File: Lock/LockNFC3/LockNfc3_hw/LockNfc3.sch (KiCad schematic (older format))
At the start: 118 parts, among them Q1 IRLML9303, Q2 BC817, Q3 IRLML6302, Q4 IRLML6302, Q5 IRLML6302, Q6 LED_RGB, Q7 LED_RGB, Q8 LED_RGB, SW1 SS9, SW2 BUTTON, SW3 BUTTON, SW4 BUTTON

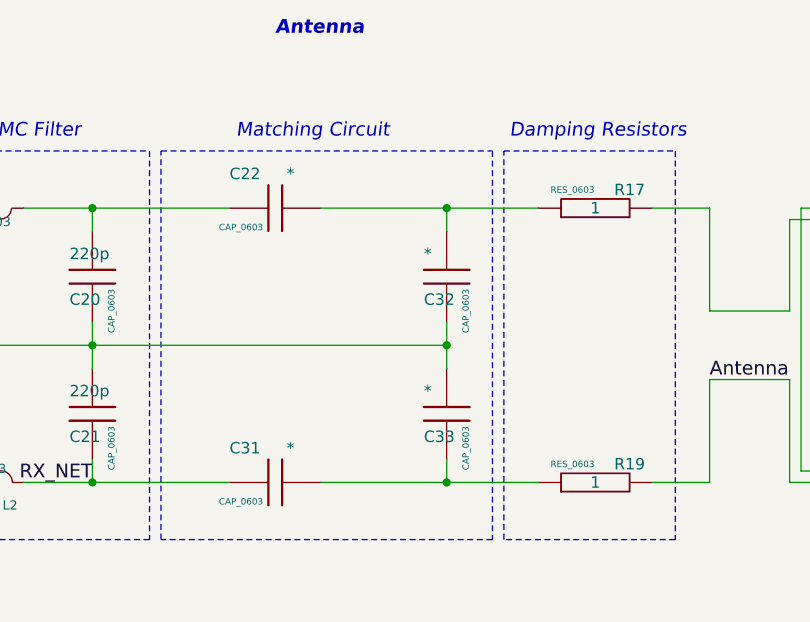
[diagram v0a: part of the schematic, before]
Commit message: * Capacitors values added
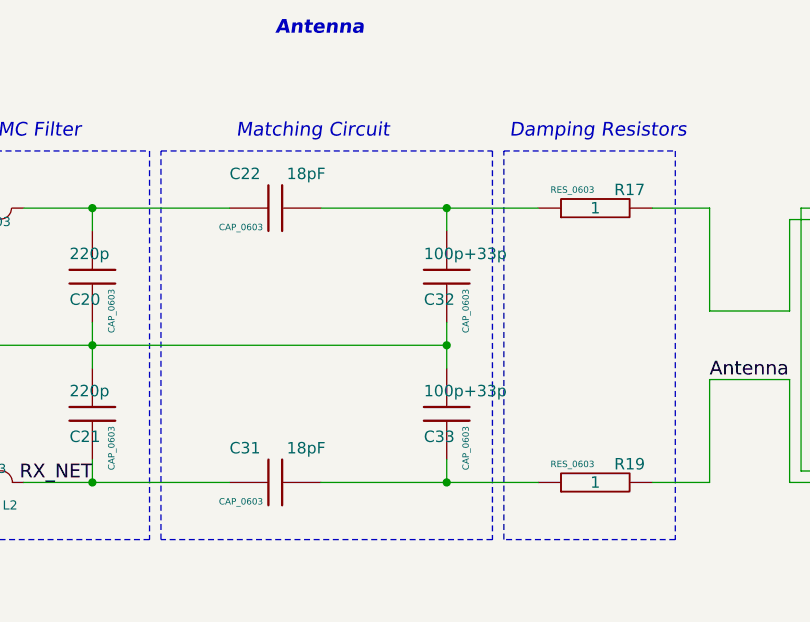
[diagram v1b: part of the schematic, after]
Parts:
- C22, C31: value * -> 18pF
- C32, C33: value * -> 100p+33p
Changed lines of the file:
@@
 Sheet 1 1
 Title ""
-Date "3 dec 2014"
+Date "24 feb 2015"
 Rev ""
 Comp ""
@@
 P 14150 3200
 F 0 "C33" H 14050 3100 50  0000 L CNN
-F 1 "*" H 14050 3300 50  0000 L CNN
+F 1 "100p+33p" H 14050 3300 50  0000 L CNN
 F 2 "CAP_0603" V 14250 3050 28  0000 C BNN
 F 3 "" H 14150 3200 60  0001 C CNN
@@
 P 14150 2600
 F 0 "C32" H 14050 2500 50  0000 L CNN
-F 1 "*" H 14050 2700 50  0000 L CNN
+F 1 "100p+33p" H 14050 2700 50  0000 L CNN
 F 2 "CAP_0603" V 14250 2450 28  0000 C BNN
 F 3 "" H 14150 2600 60  0001 C CNN
@@
 P 13400 3500
 F 0 "C31" V 13250 3300 50  0000 L CNN
-F 1 "*" V 13250 3550 50  0000 L CNN
+F 1 "18pF" V 13250 3550 50  0000 L CNN
 F 2 "CAP_0603" V 13500 3350 28  0000 C BNN
 F 3 "" H 13400 3500 60  0001 C CNN
@@
 P 13400 2300
 F 0 "C22" V 13250 2100 50  0000 L CNN
-F 1 "*" V 13250 2350 50  0000 L CNN
+F 1 "18pF" V 13250 2350 50  0000 L CNN
 F 2 "CAP_0603" V 13500 2150 28  0000 C BNN
 F 3 "" H 13400 2300 60  0001 C CNN
